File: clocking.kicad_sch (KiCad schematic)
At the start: 44 parts, among them U3 TMP117xxDRV, U4 TG5032CGN, U5 LMK05318BRGZR

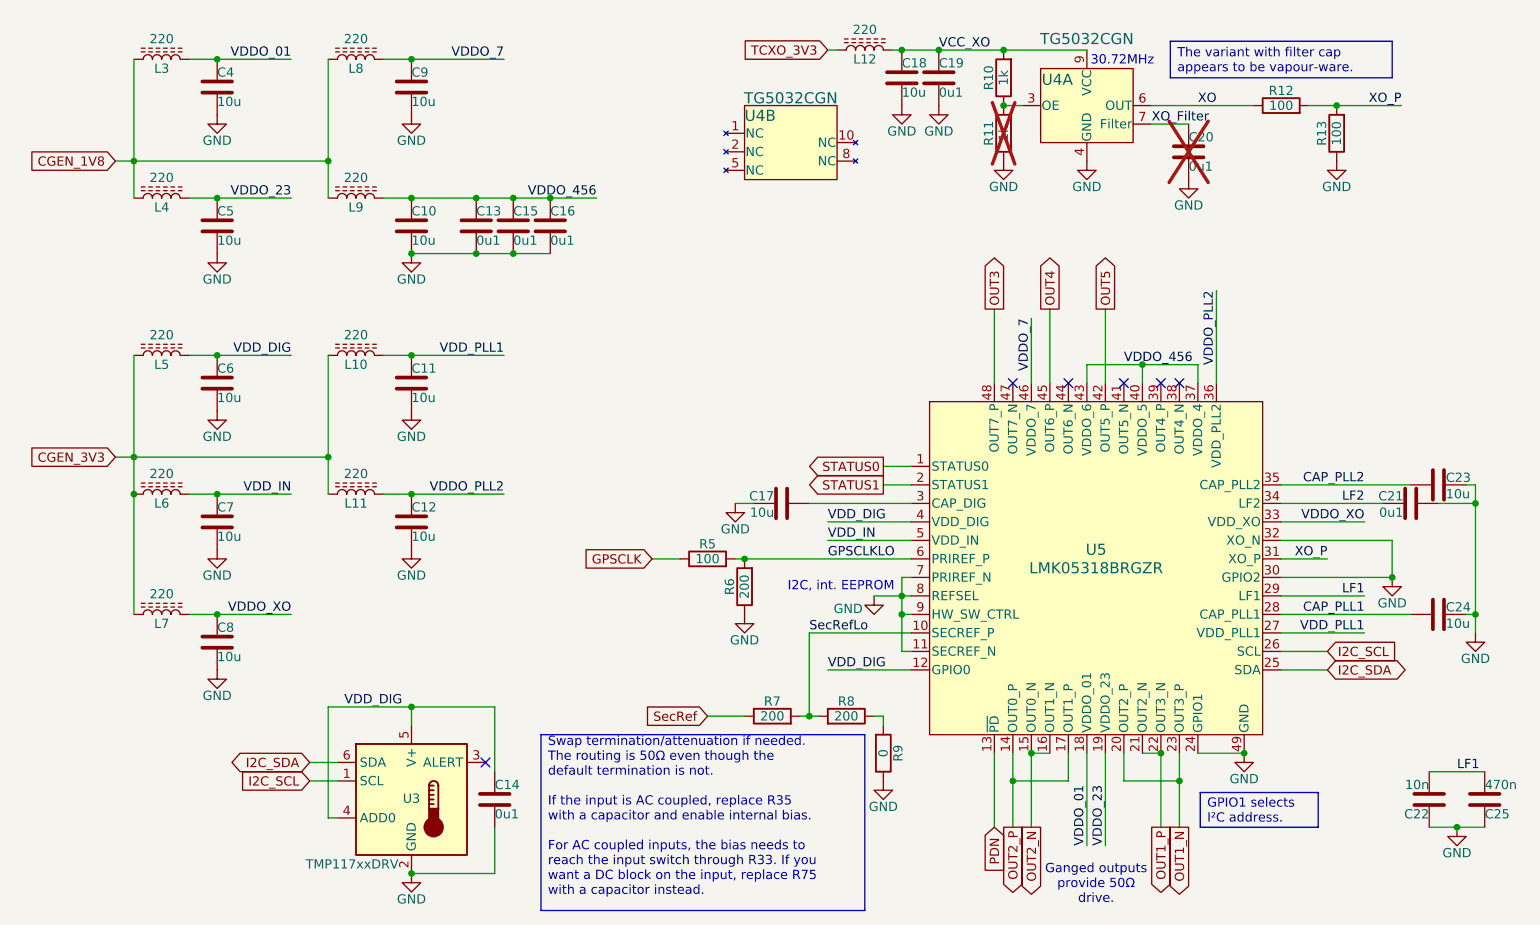
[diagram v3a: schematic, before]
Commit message: Silkscreen passes DRC.  Also we renumbered everything.
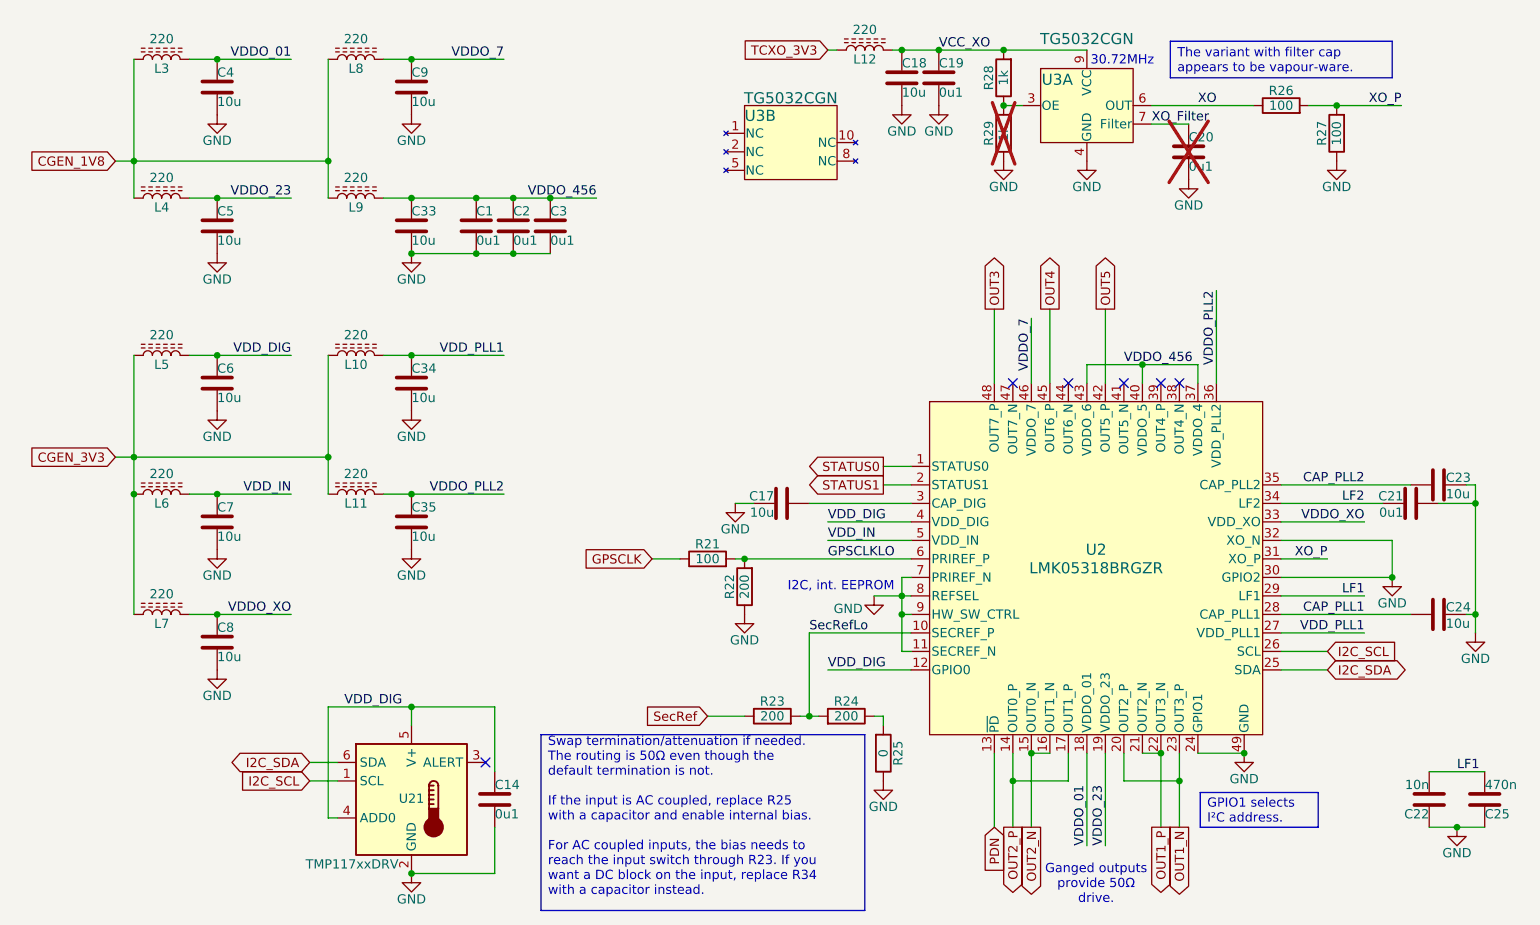
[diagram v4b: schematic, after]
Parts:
- renumbered C13 to C1, C15 to C2, C16 to C3, C10 to C33, C11 to C34, C12 to C35, R5 to R21, R6 to R22, R7 to R23, R8 to R24, R9 to R25, R12 to R26, R13 to R27, R10 to R28, R11 to R29, U5 to U2, U3 to U21, U4 to U3
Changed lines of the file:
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@@
 		)
 	)
-	(text_box "Swap termination/attenuation if needed.  The routing is 50Ω even though the default termination is not.\n\nIf the input is AC coupled, replace R35 with a capacitor and enable internal bias.\n\nFor AC coupled inputs, the bias needs to reach the input switch through R33. If you want a DC block on the input, replace R75 with a capacitor instead.\n\n"
+	(text_box "Swap termination/attenuation if needed.  The routing is 50Ω even though the default termination is not.\n\nIf the input is AC coupled, replace R25 with a capacitor and enable internal bias.\n\nFor AC coupled inputs, the bias needs to reach the input switch through R23. If you want a DC block on the input, replace R34 with a capacitor instead.\n\n"
 		(exclude_from_sim no)
 		(at 125.7299 126.9999 0)
@@
 		(on_board yes)
 		(dnp no)
-		(property "Reference" "C10"
+		(property "Reference" "C33"
 			(at 107.95 55.88 0)
 			(effects
@@
 			(project "gpsref"
 				(path "/3160ff17-81c2-4674-af97-e8d9acaf6b65/131a3728-0d51-4d75-9961-26d31d87be39"
-					(reference "C10")
+					(reference "C33")
 					(unit 1)
 				)
@@
 		(on_board yes)
 		(dnp no)
-		(property "Reference" "U3"
+		(property "Reference" "U21"
 			(at 107.95 135.763 0)
 			(effects
@@
 			(project ""
 				(path "/3160ff17-81c2-4674-af97-e8d9acaf6b65/131a3728-0d51-4d75-9961-26d31d87be39"
-					(reference "U3")
+					(reference "U21")
 					(unit 1)
 				)
@@
 		(on_board yes)
 		(dnp no)
-		(property "Reference" "R8"
+		(property "Reference" "R24"
 			(at 167.64 122.428 90)
 			(effects
@@
 			(project "gpsref"
 				(path "/3160ff17-81c2-4674-af97-e8d9acaf6b65/131a3728-0d51-4d75-9961-26d31d87be39"
-					(reference "R8")
+					(reference "R24")
 					(unit 1)
 				)
@@
 		(on_board yes)
 		(dnp no)
-		(property "Reference" "R9"
+		(property "Reference" "R25"
 			(at 174.752 129.54 90)
 			(effects
@@
 			(project "gpsref"
 				(path "/3160ff17-81c2-4674-af97-e8d9acaf6b65/131a3728-0d51-4d75-9961-26d31d87be39"
-					(reference "R9")
+					(reference "R25")
 					(unit 1)
 				)
@@
 		(on_board yes)
 		(dnp no)
-		(property "Reference" "C16"
+		(property "Reference" "C3"
 			(at 127 55.88 0)
 			(effects
@@
 			(project "gpsref"
 				(path "/3160ff17-81c2-4674-af97-e8d9acaf6b65/131a3728-0d51-4d75-9961-26d31d87be39"
-					(reference "C16")
+					(reference "C3")
 					(unit 1)
 				)
@@
 		(on_board yes)
 		(dnp no)
-		(property "Reference" "C12"
+		(property "Reference" "C35"
 			(at 107.95 96.52 0)
 			(effects
@@
 			(project "gpsref"
 				(path "/3160ff17-81c2-4674-af97-e8d9acaf6b65/131a3728-0d51-4d75-9961-26d31d87be39"
-					(reference "C12")
+					(reference "C35")
 					(unit 1)
 				)
@@
 		(on_board yes)
 		(dnp no)
-		(property "Reference" "R12"
+		(property "Reference" "R26"
 			(at 227.33 38.608 90)
 			(effects
@@
 			(project "gpsref"
 				(path "/3160ff17-81c2-4674-af97-e8d9acaf6b65/131a3728-0d51-4d75-9961-26d31d87be39"
-					(reference "R12")
+					(reference "R26")
 					(unit 1)
 				)
@@
 		(on_board yes)
 		(dnp no)
-		(property "Reference" "C15"
+		(property "Reference" "C2"
 			(at 121.92 55.88 0)
 			(effects
@@
 			(project "gpsref"
 				(path "/3160ff17-81c2-4674-af97-e8d9acaf6b65/131a3728-0d51-4d75-9961-26d31d87be39"
-					(reference "C15")
+					(reference "C2")
 					(unit 1)
 				)
@@
 		(on_board yes)
 		(dnp no)
-		(property "Reference" "C13"
+		(property "Reference" "C1"
 			(at 116.84 55.88 0)
 			(effects
@@
 			(project "gpsref"
 				(path "/3160ff17-81c2-4674-af97-e8d9acaf6b65/131a3728-0d51-4d75-9961-26d31d87be39"
-					(reference "C13")
+					(reference "C1")
 					(unit 1)
 				)
@@
 		(on_board yes)
 		(dnp no)
-		(property "Reference" "U5"
+		(property "Reference" "U2"
 			(at 201.93 101.6 0)
 			(effects
@@
 			(project "gpsref"
 				(path "/3160ff17-81c2-4674-af97-e8d9acaf6b65/131a3728-0d51-4d75-9961-26d31d87be39"
-					(reference "U5")
+					(reference "U2")
 					(unit 1)
 				)
@@
 		(on_board yes)
 		(dnp no)
-		(property "Reference" "R13"
+		(property "Reference" "R27"
 			(at 232.918 44.45 90)
 			(effects
@@
 			(project ""
 				(path "/3160ff17-81c2-4674-af97-e8d9acaf6b65/131a3728-0d51-4d75-9961-26d31d87be39"
-					(reference "R13")
+					(reference "R27")
 					(unit 1)
 				)
@@
 		(on_board yes)
 		(dnp no)
-		(property "Reference" "R5"
+		(property "Reference" "R21"
 			(at 148.59 100.838 90)
 			(effects
@@
 			(project "gpsref"
 				(path "/3160ff17-81c2-4674-af97-e8d9acaf6b65/131a3728-0d51-4d75-9961-26d31d87be39"
-					(reference "R5")
+					(reference "R21")
 					(unit 1)
 				)
@@
 		(on_board yes)
 		(dnp yes)
-		(property "Reference" "R11"
+		(property "Reference" "R29"
 			(at 187.198 44.45 90)
 			(effects
@@
 			(project "gpsref"
 				(path "/3160ff17-81c2-4674-af97-e8d9acaf6b65/131a3728-0d51-4d75-9961-26d31d87be39"
-					(reference "R11")
+					(reference "R29")
 					(unit 1)
 				)
@@
 		(on_board yes)
 		(dnp no)
-		(property "Reference" "U4"
+		(property "Reference" "U3"
 			(at 196.596 37.084 0)
 			(effects
@@
 			(project "gpsref"
 				(path "/3160ff17-81c2-4674-af97-e8d9acaf6b65/131a3728-0d51-4d75-9961-26d31d87be39"
-					(reference "U4")
+					(reference "U3")
 					(unit 1)
 				)
@@
 		(on_board yes)
 		(dnp no)
-		(property "Reference" "R7"
+		(property "Reference" "R23"
 			(at 157.48 122.428 90)
 			(effects
@@
 			(project "gpsref"
 				(path "/3160ff17-81c2-4674-af97-e8d9acaf6b65/131a3728-0d51-4d75-9961-26d31d87be39"
-					(reference "R7")
+					(reference "R23")
 					(unit 1)
 				)
@@
 		(on_board yes)
 		(dnp no)
-		(property "Reference" "R6"
+		(property "Reference" "R22"
 			(at 151.638 106.68 90)
 			(effects
@@
 			(project "gpsref"
 				(path "/3160ff17-81c2-4674-af97-e8d9acaf6b65/131a3728-0d51-4d75-9961-26d31d87be39"
-					(reference "R6")
+					(reference "R22")
 					(unit 1)
 				)
@@
 		(on_board yes)
 		(dnp no)
-		(property "Reference" "R10"
+		(property "Reference" "R28"
 			(at 187.198 36.83 90)
 			(effects
@@
 			(project "gpsref"
 				(path "/3160ff17-81c2-4674-af97-e8d9acaf6b65/131a3728-0d51-4d75-9961-26d31d87be39"
-					(reference "R10")
+					(reference "R28")
 					(unit 1)
 				)
@@
 		(on_board yes)
 		(dnp no)
-		(property "Reference" "U4"
+		(property "Reference" "U3"
 			(at 153.67 41.148 0)
 			(effects
@@
 			(project ""
 				(path "/3160ff17-81c2-4674-af97-e8d9acaf6b65/131a3728-0d51-4d75-9961-26d31d87be39"
-					(reference "U4")
+					(reference "U3")
 					(unit 2)
 				)
@@
 		(on_board yes)
 		(dnp no)
-		(property "Reference" "C11"
+		(property "Reference" "C34"
 			(at 107.95 77.47 0)
 			(effects
@@
 			(project "gpsref"
 				(path "/3160ff17-81c2-4674-af97-e8d9acaf6b65/131a3728-0d51-4d75-9961-26d31d87be39"
-					(reference "C11")
+					(reference "C34")
 					(unit 1)
 				)

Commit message: Sorting out part number assignments.
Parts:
- C1, C19, C2, C3: JLCPCB C307331 -> (none); LCSC (none) -> C307331
- C14: LCSC (none) -> C307331
- C17, C18, C23, C24, C33, C34, C35, C4, C5, C6, C7, C8, C9: JLCPCB C15525 -> (none); LCSC (none) -> C15525
- L10, L11, L12, L3, L4, L5, L6, L7, L8, L9: JLCPCB C14709 -> (none); LCSC (none) -> C14709
- R21, R26, R27: JLCPCB C25076 -> (none); LCSC (none) -> C25076
- R22: JLCPCB C25087 -> (none); LCSC (none) -> C25087
- R23: LCSC (none) -> C8218
- R24: JLCPCB C8218 -> (none); LCSC (none) -> C8218
- R28: JLCPCB C11702 -> (none); LCSC (none) -> C11702
- U2: JLCPCB C3611586 -> (none); LCSC (none) -> C3611586
- U3: JLCPCB C2891970 -> (none); LCSC (none) -> C2891970
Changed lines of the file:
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@@
 			)
 		)
-		(property "JLCPCB" "C15525"
+		(property "LCSC" "C15525"
 			(at 81.28 114.3 0)
 			(effects
@@
 			)
 		)
-		(property "JLCPCB" "C15525"
+		(property "LCSC" "C15525"
 			(at 107.95 57.15 0)
 			(effects
@@
 			)
 		)
-		(property "JLCPCB" "C15525"
+		(property "LCSC" "C15525"
 			(at 248.92 92.71 90)
 			(effects
@@
 			)
 		)
-		(property "JLCPCB" "C15525"
+		(property "LCSC" "C15525"
 			(at 248.92 110.49 90)
 			(effects
@@
 			)
 		)
-		(property "JLCPCB" "C8218"
-			(at 167.64 124.46 0)
+		(property "LCSC" "C8218"
+			(at 167.64 124.46 90)
 			(effects
 				(font
@@
 			)
 		)
-		(property "JLCPCB" ""
-			(at 172.72 129.54 0)
-			(effects
-				(font
-					(size 1.27 1.27)
-				)
-				(hide yes)
-			)
-		)
 		(pin "2"
 		)
@@
 			)
 		)
-		(property "JLCPCB" "C14709"
+		(property "LCSC" "C14709"
 			(at 73.66 110.49 90)
 			(effects
@@
 			)
 		)
-		(property "JLCPCB" "C14709"
+		(property "LCSC" "C14709"
 			(at 100.33 93.98 90)
 			(effects
@@
 			)
 		)
-		(property "JLCPCB" "C14709"
+		(property "LCSC" "C14709"
 			(at 170.18 33.02 90)
 			(effects
@@
 			)
 		)
-		(property "JLCPCB" "C307331"
+		(property "LCSC" "C307331"
 			(at 127 57.15 0)
 			(effects
@@
 			)
 		)
-		(property "JLCPCB" "C15525"
+		(property "LCSC" "C15525"
 			(at 158.75 95.25 90)
 			(effects
@@
 			)
 		)
-		(property "JLCPCB" ""
-			(at 247.65 135.89 0)
-			(effects
-				(font
-					(size 1.27 1.27)
-				)
-				(hide yes)
-			)
-		)
 		(pin "1"
 		)
@@
 			)
 		)
-		(property "JLCPCB" "C307331"
+		(property "LCSC" "C307331"
 			(at 180.34 36.83 0)
 			(effects
@@
 			)
 		)
-		(property "JLCPCB" ""
+		(property "LCSC" "C307331"
 			(at 119.38 135.89 0)
 			(effects
@@
 			)
 		)
-		(property "JLCPCB" ""
-			(at 214.63 46.99 0)
-			(effects
-				(font
-					(size 1.27 1.27)
-				)
-				(hide yes)
-			)
-		)
 		(pin "1"
 		)
@@
 			)
 		)
-		(property "JLCPCB" "C15525"
+		(property "LCSC" "C15525"
 			(at 107.95 97.79 0)
 			(effects
@@
 			)
 		)
-		(property "JLCPCB" "C14709"
+		(property "LCSC" "C14709"
 			(at 100.33 34.29 90)
 			(effects
@@
 			)
 		)
-		(property "JLCPCB" "C25076"
+		(property "LCSC" "C25076"
 			(at 227.33 40.64 90)
 			(effects
@@
 			)
 		)
-		(property "JLCPCB" "C14709"
+		(property "LCSC" "C14709"
 			(at 73.66 34.29 90)
 			(effects
@@
 			)
 		)
-		(property "JLCPCB" "C307331"
+		(property "LCSC" "C307331"
 			(at 121.92 57.15 0)
 			(effects
@@
 			)
 		)
-		(property "JLCPCB" "C307331"
+		(property "LCSC" "C307331"
 			(at 116.84 57.15 0)
 			(effects
@@
 			)
 		)
-		(property "JLCPCB" "C15525"
+		(property "LCSC" "C15525"
 			(at 107.95 38.1 0)
 			(effects
@@
 			)
 		)
-		(property "JLCPCB" "C14709"
+		(property "LCSC" "C14709"
 			(at 73.66 93.98 90)
 			(effects
@@
 			)
 		)
-		(property "JLCPCB" "C15525"
+		(property "LCSC" "C15525"
 			(at 81.28 78.74 0)
 			(effects
@@
 			)
 		)
-		(property "JLCPCB" "C15525"
+		(property "LCSC" "C15525"
 			(at 81.28 57.15 0)
 			(effects
@@
 			)
 		)
-		(property "JLCPCB" "C15525"
+		(property "LCSC" "C15525"
 			(at 175.26 36.83 0)
 			(effects
@@
 			)
 		)
-		(property "JLCPCB" "C3611586"
+		(property "LCSC" "C3611586"
 			(at 201.93 104.14 0)
 			(effects
@@
 			)
 		)
-		(property "JLCPCB" "C25076"
-			(at 234.95 44.45 0)
+		(property "LCSC" "C25076"
+			(at 234.95 44.45 90)
 			(effects
 				(font
@@
 			)
 		)
-		(property "JLCPCB" "C14709"
+		(property "LCSC" "C14709"
 			(at 73.66 74.93 90)
 			(effects
@@
 			)
 		)
-		(property "JLCPCB" "C14709"
+		(property "LCSC" "C14709"
 			(at 100.33 53.34 90)
 			(effects
@@
 			)
 		)
-		(property "JLCPCB" "C14709"
+		(property "LCSC" "C14709"
 			(at 100.33 74.93 90)
 			(effects
@@
 			)
 		)
-		(property "JLCPCB" "C25076"
-			(at 148.59 102.87 0)
+		(property "LCSC" "C25076"
+			(at 148.59 102.87 90)
 			(effects
 				(font
@@
 			)
 		)
-		(property "JLCPCB" ""
-			(at 189.23 44.45 0)
-			(effects
-				(font
-					(size 1.27 1.27)
-				)
-				(hide yes)
-			)
-		)
 		(pin "2"
 		)
@@
 			)
 		)
-		(property "JLCPCB" "C2891970"
+		(property "LCSC" "C2891970"
 			(at 200.66 40.64 0)
 			(effects
@@
 			)
 		)
-		(property "JLCPCB" ""
-			(at 157.48 124.46 0)
+		(property "LCSC" "C8218"
+			(at 157.48 124.46 90)
 			(effects
 				(font
@@
 			)
 		)
-		(property "JLCPCB" "C15525"
+		(property "LCSC" "C15525"
 			(at 81.28 97.79 0)
 			(effects
@@
 			)
 		)
-		(property "JLCPCB" "C25087"
-			(at 153.67 106.68 0)
+		(property "LCSC" "C25087"
+			(at 153.67 106.68 90)
 			(effects
 				(font
@@
 			)
 		)
-		(property "JLCPCB" "C11702"
-			(at 189.23 36.83 0)
+		(property "LCSC" "C11702"
+			(at 189.23 36.83 90)
 			(effects
 				(font
@@
 			)
 		)
-		(property "JLCPCB" "C15525"
+		(property "LCSC" "C15525"
 			(at 81.28 38.1 0)
 			(effects
@@
 			)
 		)
-		(property "JLCPCB" "C2891970"
+		(property "LCSC" "C2891970"
 			(at 160.02 45.72 0)
 			(effects
@@
 			)
 		)
-		(property "JLCPCB" ""
-			(at 255.27 135.89 0)
-			(effects
-				(font
-					(size 1.27 1.27)
-				)
-				(hide yes)
-			)
-		)
 		(pin "1"
 		)
@@
 			)
 		)
-		(property "JLCPCB" "C15525"
+		(property "LCSC" "C15525"
 			(at 107.95 78.74 0)
 			(effects
@@
 			)
 		)
-		(property "JLCPCB" ""
-			(at 245.11 95.25 0)
-			(effects
-				(font
-					(size 1.27 1.27)
-				)
-				(hide yes)
-			)
-		)
 		(pin "1"
 		)
@@
 			)
 		)
-		(property "JLCPCB" "C14709"
+		(property "LCSC" "C14709"
 			(at 73.66 53.34 90)
 			(effects

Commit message: Schematic updates for revision mostly done.
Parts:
- removed C19: 0u1, Capacitor_SMD:C_0402_1005Metric, symbol Device:C
- removed C20: 0u1, Parts:C0704, symbol Device:C
- removed R23, R24: 200, Resistor_SMD:R_0603_1608Metric, symbol Device:R
- removed R25: 0, Resistor_SMD:R_0603_1608Metric, symbol Device:R
- removed R28, R29: 1k, Resistor_SMD:R_0402_1005Metric, symbol Device:R
- added J9: U.Fl, Parts:U.FL_Hirose_U.FL-R-SMT-1_Vertical, symbol Connector:Conn_Coaxial
- R22: value 200 -> 100; LCSC C25087 -> C25076
- renumbered C4 to C21, C9 to C22, C5 to C23, C33 to C24, C1 to C25, C2 to C27, C3 to C28, C18 to C29, C6 to C71, C34 to C72, C7 to C73, C35 to C74, C8 to C75, C14 to C76, C17 to C77, C22 to C78, C25 to C79, C23 to C91, C21 to C92, C24 to C93, L3 to L21, L4 to L22, L5 to L23, L6 to L24, L7 to L25, L8 to L26, L9 to L27, L10 to L28, L11 to L29, R26 to R23, R27 to R24
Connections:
- net TCXO_3V3 is gone; now on net +3V3: L12.1
- net GND: now also J9.2 (Ext); no longer R22.1, U2.30 (GPIO2)
- net GPSCLKLO: no longer R22.2
- net SecRefLo: now also R22.2
- net VCC_XO: now also U3.3 (OE)
- net OUT4_N: now reaches U2.44 (OUT6_N)
- net OUT3_N: now reaches U2.47 (OUT7_N)
- net CGEN_3V3 renamed +3V3
- net OUT3 renamed OUT3_P
- net OUT4 renamed OUT4_P
- net STATUS1 renamed FDEC
- net XO_Filter: no longer names the net of U3.7 (Filter)
- new net: J9.1 (In), R22.1
- new net FINC: U2.30 (GPIO2)
- no-connect marks 6 -> 5
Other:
- moved on the sheet: C25, C28, C29, C78, C79, L12, R21, U3B
